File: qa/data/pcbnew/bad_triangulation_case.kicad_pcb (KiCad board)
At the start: 2 copper layers, 0 parts

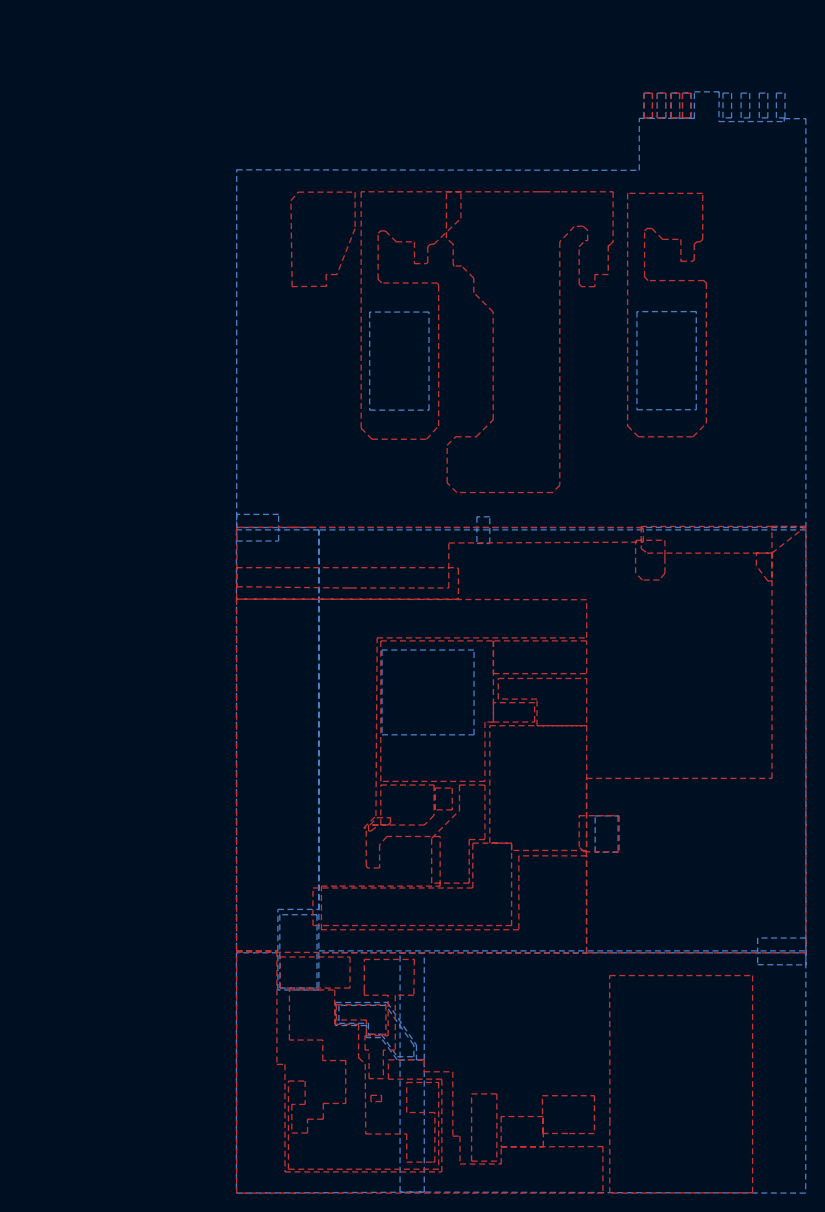
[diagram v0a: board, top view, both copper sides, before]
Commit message: feat: update kicad to 9.0.0+dfsg-1
Signed-off-by: lhdjply <lhdjply@126.com>
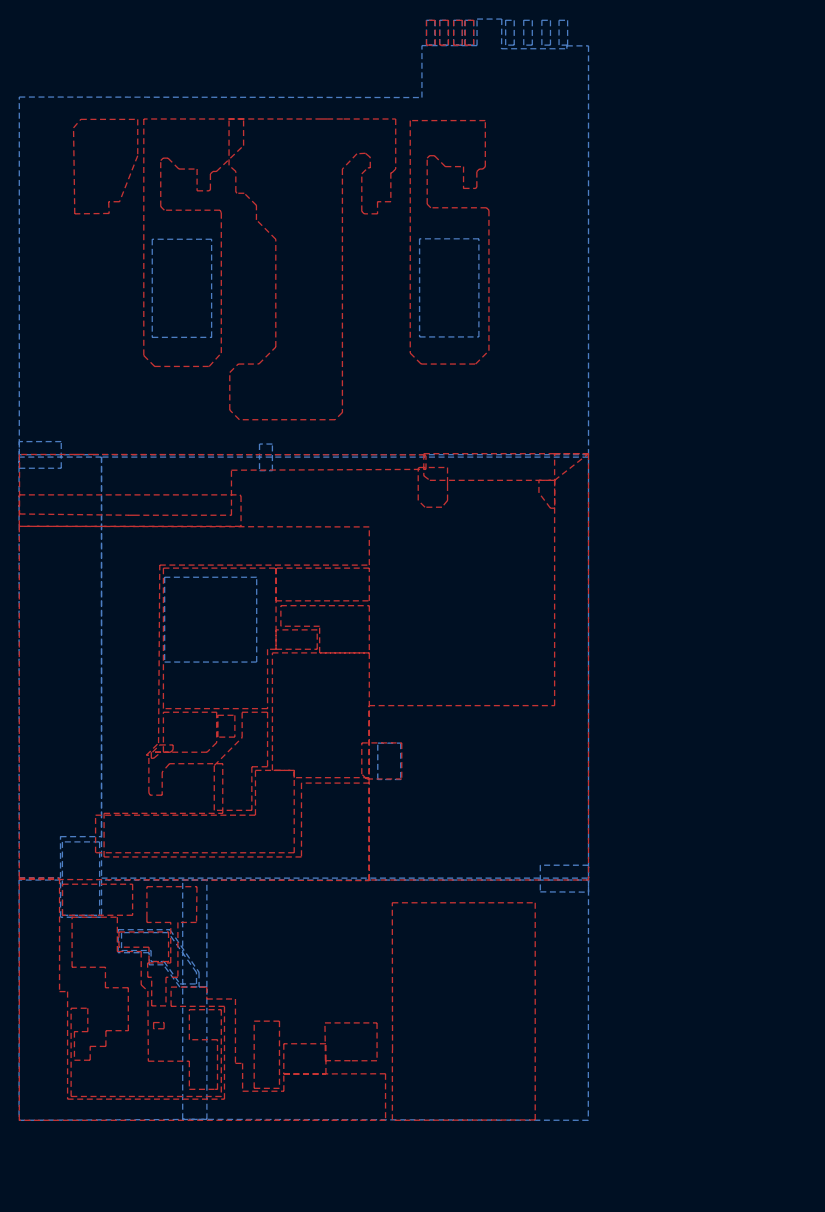
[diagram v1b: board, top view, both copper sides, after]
